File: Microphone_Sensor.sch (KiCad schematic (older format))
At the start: 23 parts, among them J7 JST-GH, U4 TS472

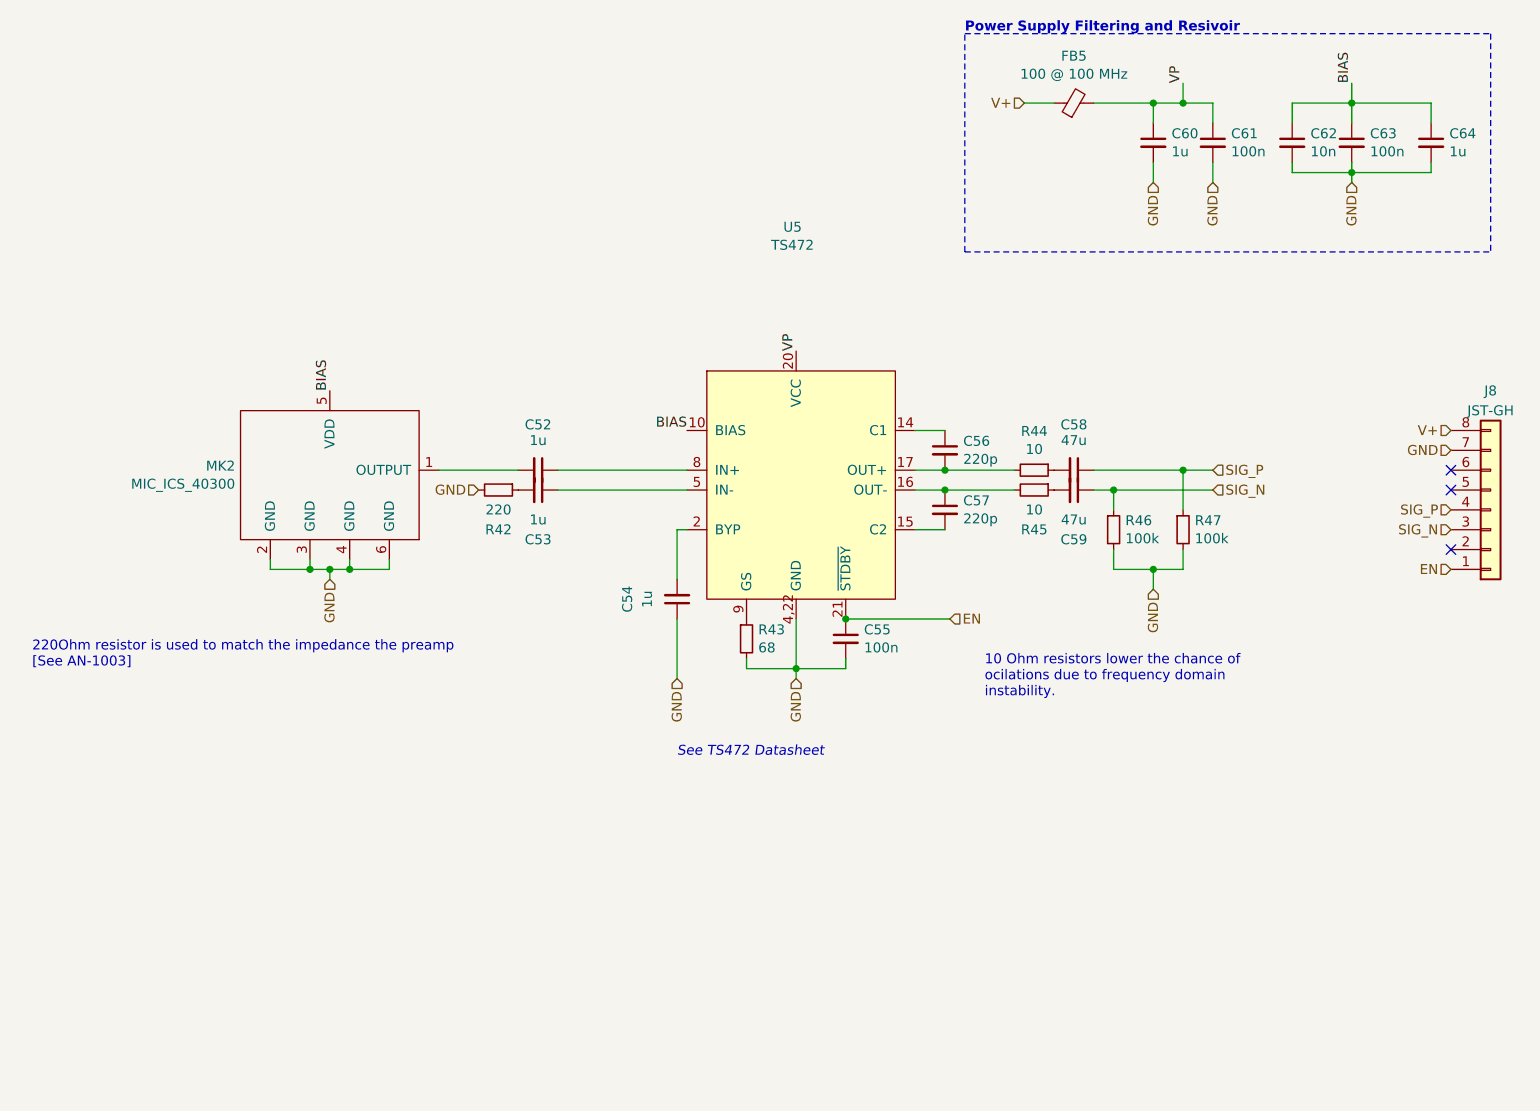
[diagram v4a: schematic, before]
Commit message: Assign footprints for all components
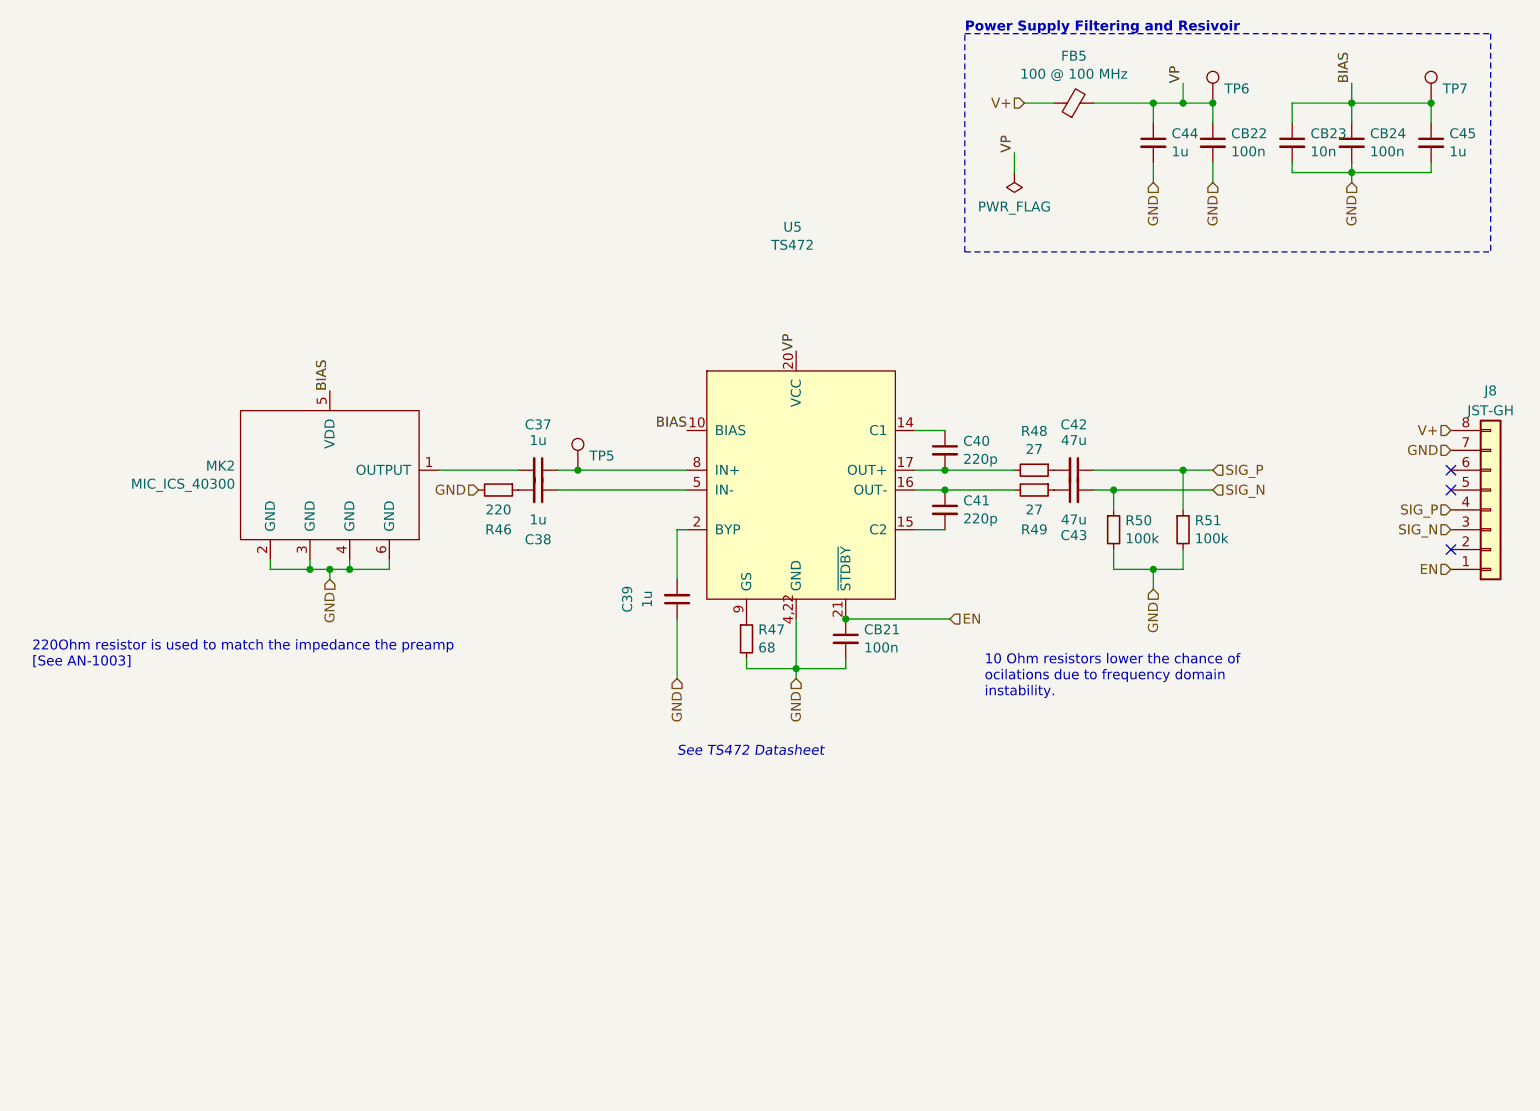
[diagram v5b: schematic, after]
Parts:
- removed C46: 47u, symbol Device:C_Small
- added C34: 47u, Capacitor_SMD:C_1206_3216Metric_Pad1.42x1.75mm_HandSolder, symbol Device:C_Small
- added TP2, TP3, TP4: TestPoint, TestPoint:TestPoint_Pad_D1.0mm, symbol Connector:TestPoint
- C28: renamed from C39; footprint (none) -> Capacitor_SMD:C_0603_1608Metric_Pad1.05x0.95mm_HandSolder; MPN (none) -> C0603C105K8RACTU; Mfr. (none) -> KEMET
- C29: renamed from C40; footprint (none) -> Capacitor_SMD:C_0603_1608Metric_Pad1.05x0.95mm_HandSolder; MPN (none) -> C0603C105K8RACTU; Mfr. (none) -> KEMET
- C30: renamed from C41; footprint (none) -> Capacitor_SMD:C_0603_1608Metric_Pad1.05x0.95mm_HandSolder; MPN (none) -> C0603C105K8RACTU; Mfr. (none) -> KEMET
- C31: renamed from C43; footprint (none) -> Capacitor_SMD:C_0603_1608Metric_Pad1.05x0.95mm_HandSolder
- C32: renamed from C44; footprint (none) -> Capacitor_SMD:C_0603_1608Metric_Pad1.05x0.95mm_HandSolder
- C33: renamed from C45; footprint (none) -> Capacitor_SMD:C_1206_3216Metric_Pad1.42x1.75mm_HandSolder; MPN (none) -> GRM31CR60J107KE39K; Mfr. (none) -> Murata Electronics; Notes (none) -> Specified 47u but that is min. (>47u is better)
- C35: renamed from C47; footprint (none) -> Capacitor_SMD:C_0603_1608Metric_Pad1.05x0.95mm_HandSolder; MPN (none) -> C0603C105K8RACTU; Mfr. (none) -> KEMET
- C36: renamed from C51; footprint (none) -> Capacitor_SMD:C_0603_1608Metric_Pad1.05x0.95mm_HandSolder; MPN (none) -> C0603C105K8RACTU; Mfr. (none) -> KEMET
- CB17: renamed from C42; footprint (none) -> Capacitor_SMD:C_0603_1608Metric_Pad1.05x0.95mm_HandSolder
- CB18: renamed from C48; footprint (none) -> Capacitor_SMD:C_0603_1608Metric_Pad1.05x0.95mm_HandSolder
- CB19: renamed from C49; footprint (none) -> Capacitor_SMD:C_0603_1608Metric_Pad1.05x0.95mm_HandSolder
- CB20: renamed from C50; footprint (none) -> Capacitor_SMD:C_0603_1608Metric_Pad1.05x0.95mm_HandSolder
- FB4: footprint (none) -> Inductor_SMD:L_0603_1608Metric_Pad1.05x0.95mm_HandSolder; MPN (none) -> BLM18KG101TZ1D; Mfr. (none) -> Murata Electronics
- J7: footprint (none) -> Connector_Molex:Molex_PicoBlade_53047-0810_1x08_P1.25mm_Vertical
- R40: renamed from R36; footprint (none) -> Resistor_SMD:R_0603_1608Metric_Pad1.05x0.95mm_HandSolder; MFN (none) -> ERJ-3RBD2200V; Mfr. (none) -> Panasonic
- R41: renamed from R37; footprint (none) -> Resistor_SMD:R_0603_1608Metric_Pad1.05x0.95mm_HandSolder
- R42: renamed from R38; value 10 -> 27; footprint (none) -> Resistor_SMD:R_0603_1608Metric_Pad1.05x0.95mm_HandSolder
- R43: renamed from R39; value 10 -> 27; footprint (none) -> Resistor_SMD:R_0603_1608Metric_Pad1.05x0.95mm_HandSolder
- R44: renamed from R40; footprint (none) -> Resistor_SMD:R_0603_1608Metric_Pad1.05x0.95mm_HandSolder; MPN (none) -> RC0603FR-07100KL; Mfr. (none) -> Yageo
- R45: renamed from R41; footprint (none) -> Resistor_SMD:R_0603_1608Metric_Pad1.05x0.95mm_HandSolder; MPN (none) -> RC0603FR-07100KL; Mfr. (none) -> Yageo
- U4: footprint (none) -> Package_DFN_QFN:VQFN-24-1EP_4x4mm_P0.5mm_EP2.45x2.45mm_ThermalVias
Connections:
- net BIAS: now also TP4.1
- net SIG_N: now also C34.2
- net VP: now also TP3.1
- net at C28.1, U4.8 (IN+): now also TP2.1
- net at R43.1: now also C34.1

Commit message: Change voltage polarity diode
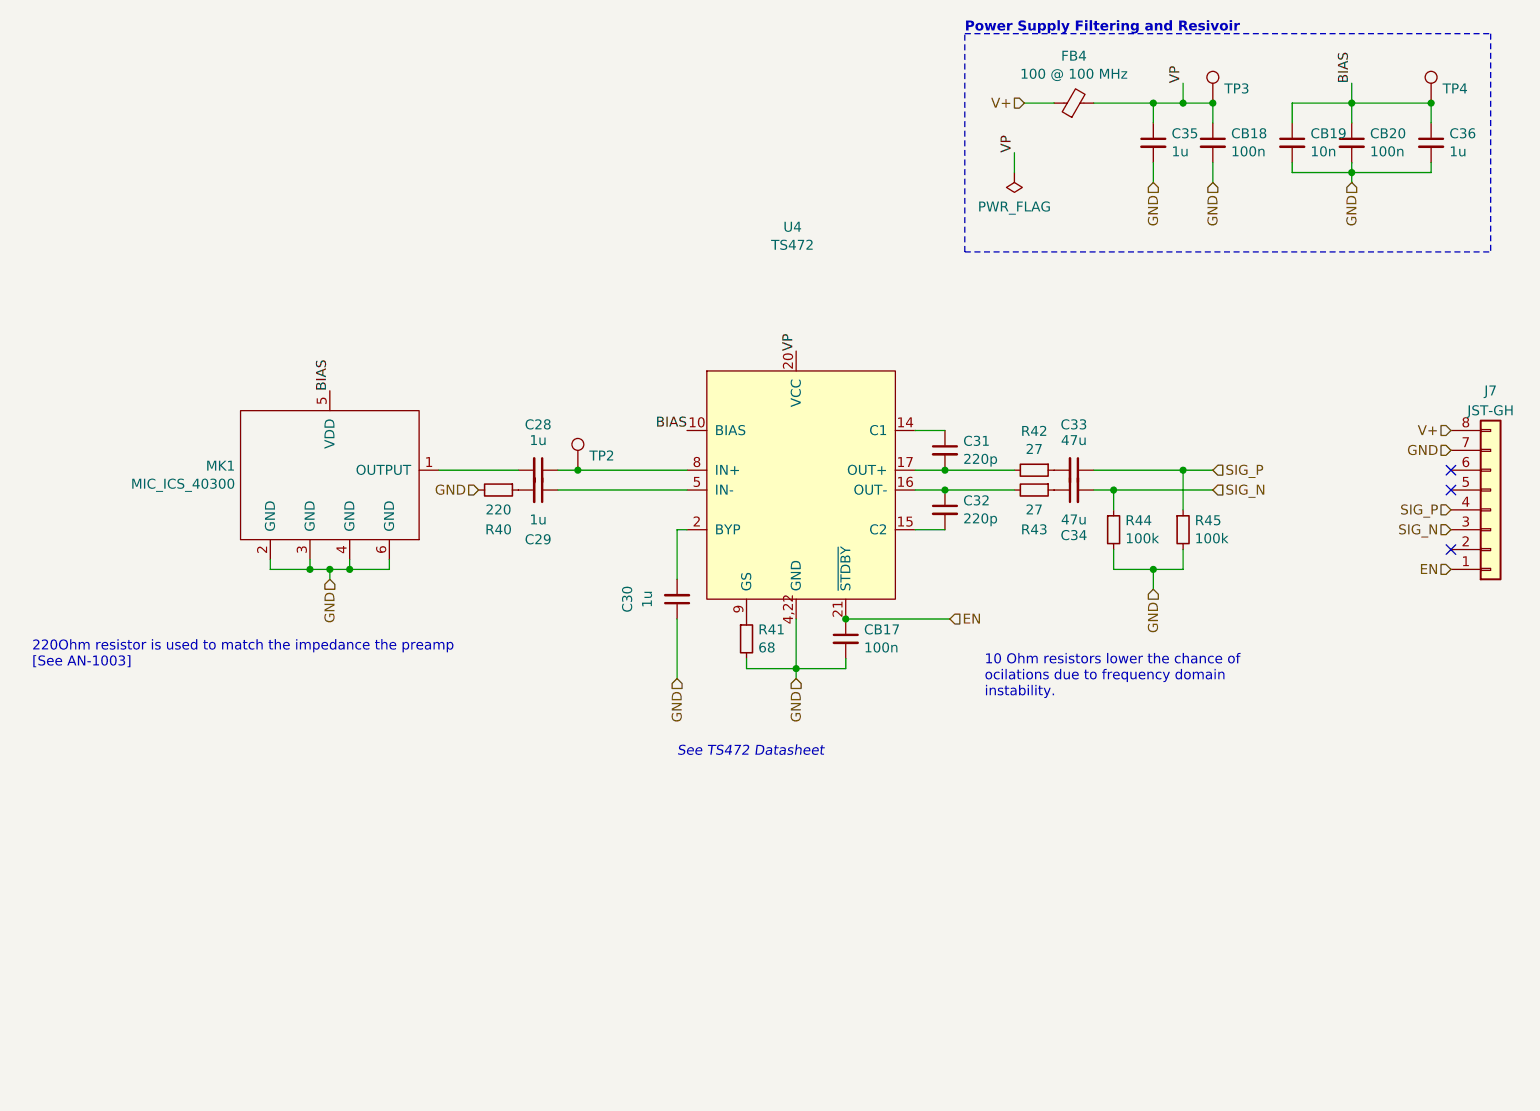
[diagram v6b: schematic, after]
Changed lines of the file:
@@
 $Descr A4 11693 8268
 encoding utf-8
-Sheet 12 15
+Sheet 11 15
 Title "Kleinvoet"
 Date "2020-06-11"
@@
 AR Path="/5EE5ECAD/5EF21991/5EEDE2AE" Ref="MK?"  Part="1"
 AR Path="/5EE5ECAD/5EF33EA2/5EEDE2AE" Ref="MK2"  Part="1"
-F 0 "MK2" H 3623 2921 50  0000 R CNN
+F 0 "MK1" H 3623 2921 50  0000 R CNN
 F 1 "MIC_ICS_40300" H 3623 2830 50  0000 R CNN
 F 2 "grootvoet:MEMS_Mic_ICS-40300" H 4100 2800 50  0001 C CNN
@@
 AR Path="/5EE5ECAD/5EF21991/5EEDEA2B" Ref="C?"  Part="1"
 AR Path="/5EE5ECAD/5EF33EA2/5EEDEA2B" Ref="C37"  Part="1"
-F 0 "C37" V 4921 2900 50  0000 C CNN
+F 0 "C28" V 4921 2900 50  0000 C CNN
 F 1 "1u" V 5000 2900 50  0000 C CNN
 F 2 "Capacitor_SMD:C_0603_1608Metric_Pad1.05x0.95mm_HandSolder" H 5150 2900 50  0001 C CNN
@@
 AR Path="/5EE5ECAD/5EF21991/5EEE2D96" Ref="J?"  Part="1"
 AR Path="/5EE5ECAD/5EF33EA2/5EEE2D96" Ref="J8"  Part="1"
-F 0 "J8" H 9950 2500 50  0000 C CNN
+F 0 "J7" H 9950 2500 50  0000 C CNN
 F 1 "JST-GH" H 9950 2600 50  0000 C CNN
 F 2 "Connector_Molex:Molex_PicoBlade_53047-0810_1x08_P1.25mm_Vertical" H 9950 3100 50  0001 C CNN
@@
 AR Path="/5EE5ECAD/5EF21991/5EEFDD4C" Ref="CB?"  Part="1"
 AR Path="/5EE5ECAD/5EF33EA2/5EEFDD4C" Ref="CB24"  Part="1"
-F 0 "CB24" H 9342 1296 50  0000 L CNN
+F 0 "CB20" H 9342 1296 50  0000 L CNN
 F 1 "100n" H 9342 1205 50  0000 L CNN
 F 2 "Capacitor_SMD:C_0603_1608Metric_Pad1.05x0.95mm_HandSolder" H 9250 1250 50  0001 C CNN
@@
 AR Path="/5EE5ECAD/5EF21991/5EF35019" Ref="FB?"  Part="1"
 AR Path="/5EE5ECAD/5EF33EA2/5EF35019" Ref="FB5"  Part="1"
-F 0 "FB5" V 8087 1050 50  0000 C CNN
+F 0 "FB4" V 8087 1050 50  0000 C CNN
 F 1 "100 @ 100 MHz" V 7996 1050 50  0000 C CNN
 F 2 "Inductor_SMD:L_0603_1608Metric_Pad1.05x0.95mm_HandSolder" V 7780 1050 50  0001 C CNN
@@
 AR Path="/5EE5ECAD/5EF21991/5EE1252E" Ref="U?"  Part="1"
 AR Path="/5EE5ECAD/5EF33EA2/5EE1252E" Ref="U5"  Part="1"
-F 0 "U5" H 6432 4225 50  0000 C CNN
+F 0 "U4" H 6432 4225 50  0000 C CNN
 F 1 "TS472" H 6432 4134 50  0000 C CNN
 F 2 "Package_DFN_QFN:VQFN-24-1EP_4x4mm_P0.5mm_EP2.45x2.45mm_ThermalVias" H 6900 3550 50  0001 C CNN
@@
 AR Path="/5EE5ECAD/5EF21991/5EE150A7" Ref="R?"  Part="1"
 AR Path="/5EE5ECAD/5EF33EA2/5EE150A7" Ref="R46"  Part="1"
-F 0 "R46" V 5150 3000 50  0000 C CNN
+F 0 "R40" V 5150 3000 50  0000 C CNN
 F 1 "220" V 5050 3000 50  0000 C CNN
 F 2 "Resistor_SMD:R_0603_1608Metric_Pad1.05x0.95mm_HandSolder" H 4950 3000 50  0001 C CNN
@@
 AR Path="/5EE5ECAD/5EF21991/5EE19951" Ref="C?"  Part="1"
 AR Path="/5EE5ECAD/5EF33EA2/5EE19951" Ref="C38"  Part="1"
-F 0 "C38" V 5400 3000 50  0000 C CNN
+F 0 "C29" V 5400 3000 50  0000 C CNN
 F 1 "1u" V 5300 3000 50  0000 C CNN
 F 2 "Capacitor_SMD:C_0603_1608Metric_Pad1.05x0.95mm_HandSolder" H 5150 3000 50  0001 C CNN
@@
 AR Path="/5EE5ECAD/5EF21991/5EE1EACE" Ref="C?"  Part="1"
 AR Path="/5EE5ECAD/5EF33EA2/5EE1EACE" Ref="C39"  Part="1"
-F 0 "C39" V 6100 3550 50  0000 C CNN
+F 0 "C30" V 6100 3550 50  0000 C CNN
 F 1 "1u" V 6000 3550 50  0000 C CNN
 F 2 "Capacitor_SMD:C_0603_1608Metric_Pad1.05x0.95mm_HandSolder" H 5850 3550 50  0001 C CNN
@@
 AR Path="/5EE5ECAD/5EF21991/5EE21893" Ref="R?"  Part="1"
 AR Path="/5EE5ECAD/5EF33EA2/5EE21893" Ref="R47"  Part="1"
-F 0 "R47" H 6259 3796 50  0000 L CNN
+F 0 "R41" H 6259 3796 50  0000 L CNN
 F 1 "68" H 6259 3705 50  0000 L CNN
 F 2 "Resistor_SMD:R_0603_1608Metric_Pad1.05x0.95mm_HandSolder" H 6200 3750 50  0001 C CNN
@@
 AR Path="/5EE5ECAD/5EF21991/5EE3D7C0" Ref="C?"  Part="1"
 AR Path="/5EE5ECAD/5EF33EA2/5EE3D7C0" Ref="C44"  Part="1"
-F 0 "C44" H 8342 1296 50  0000 L CNN
+F 0 "C35" H 8342 1296 50  0000 L CNN
 F 1 "1u" H 8342 1205 50  0000 L CNN
 F 2 "Capacitor_SMD:C_0603_1608Metric_Pad1.05x0.95mm_HandSolder" H 8250 1250 50  0001 C CNN
@@
 AR Path="/5EE5ECAD/5EF21991/5EE4D182" Ref="C?"  Part="1"
 AR Path="/5EE5ECAD/5EF33EA2/5EE4D182" Ref="C45"  Part="1"
-F 0 "C45" H 9742 1296 50  0000 L CNN
+F 0 "C36" H 9742 1296 50  0000 L CNN
 F 1 "1u" H 9742 1205 50  0000 L CNN
 F 2 "Capacitor_SMD:C_0603_1608Metric_Pad1.05x0.95mm_HandSolder" H 9650 1250 50  0001 C CNN
@@
 AR Path="/5EE5ECAD/5EF21991/5EE3C381" Ref="CB?"  Part="1"
 AR Path="/5EE5ECAD/5EF33EA2/5EE3C381" Ref="CB22"  Part="1"
-F 0 "CB22" H 8642 1296 50  0000 L CNN
+F 0 "CB18" H 8642 1296 50  0000 L CNN
 F 1 "100n" H 8642 1205 50  0000 L CNN
 F 2 "Capacitor_SMD:C_0603_1608Metric_Pad1.05x0.95mm_HandSolder" H 8550 1250 50  0001 C CNN
@@
 AR Path="/5EE5ECAD/5EF21991/5EE64CD6" Ref="C?"  Part="1"
 AR Path="/5EE5ECAD/5EF33EA2/5EE64CD6" Ref="C41"  Part="1"
-F 0 "C41" H 7292 3146 50  0000 L CNN
+F 0 "C32" H 7292 3146 50  0000 L CNN
 F 1 "220p" H 7292 3055 50  0000 L CNN
 F 2 "Capacitor_SMD:C_0603_1608Metric_Pad1.05x0.95mm_HandSolder" H 7200 3100 50  0001 C CNN
@@
 AR Path="/5EE5ECAD/5EF21991/5EE65504" Ref="C?"  Part="1"
 AR Path="/5EE5ECAD/5EF33EA2/5EE65504" Ref="C40"  Part="1"
-F 0 "C40" H 7292 2846 50  0000 L CNN
+F 0 "C31" H 7292 2846 50  0000 L CNN
 F 1 "220p" H 7292 2755 50  0000 L CNN
 F 2 "Capacitor_SMD:C_0603_1608Metric_Pad1.05x0.95mm_HandSolder" H 7200 2800 50  0001 C CNN
@@
 AR Path="/5EE5ECAD/5EF21991/5EE68FFE" Ref="R?"  Part="1"
 AR Path="/5EE5ECAD/5EF33EA2/5EE68FFE" Ref="R50"  Part="1"
-F 0 "R50" H 8109 3246 50  0000 L CNN
+F 0 "R44" H 8109 3246 50  0000 L CNN
 F 1 "100k" H 8109 3155 50  0000 L CNN
 F 2 "Resistor_SMD:R_0603_1608Metric_Pad1.05x0.95mm_HandSolder" H 8050 3200 50  0001 C CNN
@@
 AR Path="/5EE5ECAD/5EF21991/5EE699A6" Ref="R?"  Part="1"
 AR Path="/5EE5ECAD/5EF33EA2/5EE699A6" Ref="R51"  Part="1"
-F 0 "R51" H 8459 3246 50  0000 L CNN
+F 0 "R45" H 8459 3246 50  0000 L CNN
 F 1 "100k" H 8459 3155 50  0000 L CNN
 F 2 "Resistor_SMD:R_0603_1608Metric_Pad1.05x0.95mm_HandSolder" H 8400 3200 50  0001 C CNN
@@
 AR Path="/5EE5ECAD/5EF21991/5EE840BE" Ref="R?"  Part="1"
 AR Path="/5EE5ECAD/5EF33EA2/5EE840BE" Ref="R48"  Part="1"
-F 0 "R48" V 7454 2900 50  0000 C CNN
+F 0 "R42" V 7454 2900 50  0000 C CNN
 F 1 "27" V 7545 2900 50  0000 C CNN
 F 2 "Resistor_SMD:R_0603_1608Metric_Pad1.05x0.95mm_HandSolder" H 7650 2900 50  0001 C CNN
@@
 AR Path="/5EE5ECAD/5EF21991/5EE845A7" Ref="R?"  Part="1"
 AR Path="/5EE5ECAD/5EF33EA2/5EE845A7" Ref="R49"  Part="1"
-F 0 "R49" V 7850 3000 50  0000 C CNN
+F 0 "R43" V 7850 3000 50  0000 C CNN
 F 1 "27" V 7750 3000 50  0000 C CNN
 F 2 "Resistor_SMD:R_0603_1608Metric_Pad1.05x0.95mm_HandSolder" H 7650 3000 50  0001 C CNN
@@
 AR Path="/5EE5ECAD/5EF21991/5EE94347" Ref="C?"  Part="1"
 AR Path="/5EE5ECAD/5EF33EA2/5EE94347" Ref="C42"  Part="1"
-F 0 "C42" V 7621 2900 50  0000 C CNN
+F 0 "C33" V 7621 2900 50  0000 C CNN
 F 1 "47u" V 7700 2900 50  0000 C CNN
 F 2 "Capacitor_SMD:C_1206_3216Metric_Pad1.42x1.75mm_HandSolder" H 7850 2900 50  0001 C CNN
@@
 AR Path="/5EE5ECAD/5EF21991/5EEDB218" Ref="CB?"  Part="1"
 AR Path="/5EE5ECAD/5EF33EA2/5EEDB218" Ref="CB21"  Part="1"
-F 0 "CB21" H 6792 3796 50  0000 L CNN
+F 0 "CB17" H 6792 3796 50  0000 L CNN
 F 1 "100n" H 6792 3705 50  0000 L CNN
 F 2 "Capacitor_SMD:C_0603_1608Metric_Pad1.05x0.95mm_HandSolder" H 6700 3750 50  0001 C CNN
@@
 AR Path="/5EE5ECAD/5EF21991/5EEE5C9C" Ref="CB?"  Part="1"
 AR Path="/5EE5ECAD/5EF33EA2/5EEE5C9C" Ref="CB23"  Part="1"
-F 0 "CB23" H 9042 1296 50  0000 L CNN
+F 0 "CB19" H 9042 1296 50  0000 L CNN
 F 1 "10n" H 9042 1205 50  0000 L CNN
 F 2 "Capacitor_SMD:C_0603_1608Metric_Pad1.05x0.95mm_HandSolder" H 8950 1250 50  0001 C CNN
@@
 AR Path="/5EE5ECAD/5EECE6B8/5F1831E4" Ref="#FLG01"  Part="1"
 AR Path="/5EE5ECAD/5EF33EA2/5F1831E4" Ref="#FLG02"  Part="1"
-F 0 "#FLG02" H 7550 1475 50  0001 C CNN
+F 0 "#FLG01" H 7550 1475 50  0001 C CNN
 F 1 "PWR_FLAG" H 7550 1573 50  0000 C CNN
 F 2 "" H 7550 1400 50  0001 C CNN
@@
 AR Path="/5EE5ECAD/5EF21991/5F1F0F4E" Ref="C?"  Part="1"
 AR Path="/5EE5ECAD/5EF33EA2/5F1F0F4E" Ref="C43"  Part="1"
-F 0 "C43" V 7621 3000 50  0000 C CNN
+F 0 "C34" V 7621 3000 50  0000 C CNN
 F 1 "47u" V 7700 3000 50  0000 C CNN
 F 2 "Capacitor_SMD:C_1206_3216Metric_Pad1.42x1.75mm_HandSolder" H 7850 3000 50  0001 C CNN
@@
 AR Path="/5EE5ECAD/5EECE6B8/5F1557AF" Ref="TP2"  Part="1"
 AR Path="/5EE5ECAD/5EF33EA2/5F1557AF" Ref="TP5"  Part="1"
-F 0 "TP5" H 5408 2972 50  0000 L CNN
+F 0 "TP2" H 5408 2972 50  0000 L CNN
 F 1 "TestPoint" H 5408 2927 50  0001 L CNN
 F 2 "TestPoint:TestPoint_Pad_D1.0mm" H 5550 2900 50  0001 C CNN
@@
 AR Path="/5EE5ECAD/5EECE6B8/5F157F47" Ref="TP3"  Part="1"
 AR Path="/5EE5ECAD/5EF33EA2/5F157F47" Ref="TP6"  Part="1"
-F 0 "TP6" H 8608 1122 50  0000 L CNN
+F 0 "TP3" H 8608 1122 50  0000 L CNN
 F 1 "TestPoint" H 8608 1077 50  0001 L CNN
 F 2 "TestPoint:TestPoint_Pad_D1.0mm" H 8750 1050 50  0001 C CNN
@@
 AR Path="/5EE5ECAD/5EECE6B8/5F15842C" Ref="TP4"  Part="1"
 AR Path="/5EE5ECAD/5EF33EA2/5F15842C" Ref="TP7"  Part="1"
-F 0 "TP7" H 9708 1122 50  0000 L CNN
+F 0 "TP4" H 9708 1122 50  0000 L CNN
 F 1 "TestPoint" H 9708 1077 50  0001 L CNN
 F 2 "TestPoint:TestPoint_Pad_D1.0mm" H 9850 1050 50  0001 C CNN
